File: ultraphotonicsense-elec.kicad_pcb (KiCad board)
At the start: 2 copper layers, 83 x 38 mm, 79 parts, among them J1 Conn_Debug, J10 Conn_01x04, J11 Conn_01x04, J12 Conn_01x04, J13 Conn_01x04, J2 Conn_01x05, J3 Conn_01x05, J4 Conn_01x05, J5 Conn_01x05, J6 Conn_01x05, J7 Conn_01x05, J8 Conn_01x05, J9 Conn_01x05, P1 CAN_conn, P2 CAN_conn, Q1 BSS138, Q2 BSS138, Q3 BSS138, Q4 BSS138, Q5 BSS138, U1 TXB0108PW, U2 74HC164, U3 TCAN332, U4 LD1117S50TR_SOT223, U5 LD1117S33TR_SOT223, U6 LP38693MP-ADJ, U7 STM32F303K8Tx, Y1 Crystal

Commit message: Added RS refs
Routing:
- net GND: track 369.8 -> 380.7 mm, vias 8 -> 10
- net +3V3: track 151.2 -> 152.2 mm
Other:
- net class Default: clearance 0.2 -> 0.4
- rule trace_clearance: 0.2 -> 0.4
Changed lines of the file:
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@@
     (thickness 1.6)
     (drawings 30)
-    (tracks 756)
+    (tracks 763)
     (zones 0)
     (modules 79)
@@
     (user_trace_width 1)
     (user_trace_width 2)
-    (trace_clearance 0.2)
+    (trace_clearance 0.4)
     (zone_clearance 0.508)
     (zone_45_only no)
@@
   (net 61 "Net-(P1-Pad4)")
   (net_class Default "Ceci est la Netclass par défaut."
-    (clearance 0.2)
+    (clearance 0.4)
     (trace_width 0.25)
     (via_dia 0.8)
@@
   (segment (start 58.05 62.75) (end 59.050001 61.749999) (width 1) (layer F.Cu) (net 1))
   (segment (start 59.050001 55.350001) (end 58.55 54.85) (width 1) (layer F.Cu) (net 1))
+  (via (at 49.911107 59.581109) (size 0.8) (drill 0.4) (layers F.Cu B.Cu) (net 1))
+  (segment (start 48.55 62.75) (end 49.911107 61.388893) (width 1) (layer F.Cu) (net 1))
+  (segment (start 49.911107 61.388893) (end 49.911107 59.581109) (width 1) (layer F.Cu) (net 1))
+  (via (at 49.05 52.85) (size 0.8) (drill 0.4) (layers F.Cu B.Cu) (net 1))
+  (segment (start 49.05 52.85) (end 49.05 58.720002) (width 1) (layer B.Cu) (net 1))
+  (segment (start 49.05 58.720002) (end 49.911107 59.581109) (width 1) (layer B.Cu) (net 1))
   (segment (start 56.25 59.15) (end 56.25 52.85) (width 1) (layer F.Cu) (net 2))
   (segment (start 54.45 60.95) (end 56.25 59.15) (width 1) (layer F.Cu) (net 2))
@@
   (via (at 43 60.5) (size 0.8) (drill 0.4) (layers F.Cu B.Cu) (net 2))
   (segment (start 41.4625 60.5) (end 43 60.5) (width 0.25) (layer F.Cu) (net 2))
-  (segment (start 49.58 60.5) (end 51.5 58.58) (width 0.25) (layer B.Cu) (net 2))
-  (segment (start 43 60.5) (end 49.58 60.5) (width 0.25) (layer B.Cu) (net 2))
   (segment (start 72.5 49.5) (end 73.75 48.25) (width 0.25) (layer F.Cu) (net 2))
   (segment (start 74.725 48.725) (end 74.725 49.7) (width 0.25) (layer F.Cu) (net 2))
@@
   (via (at 57.749991 58.948616) (size 0.8) (drill 0.4) (layers F.Cu B.Cu) (net 2))
   (segment (start 58.315676 58.948616) (end 57.749991 58.948616) (width 0.5) (layer B.Cu) (net 2))
+  (segment (start 50.382082 60.899999) (end 51.5 59.782081) (width 0.25) (layer B.Cu) (net 2))
+  (segment (start 51.5 59.782081) (end 51.5 58.58) (width 0.25) (layer B.Cu) (net 2))
+  (segment (start 43.399999 60.899999) (end 50.382082 60.899999) (width 0.25) (layer B.Cu) (net 2))
+  (segment (start 43 60.5) (end 43.399999 60.899999) (width 0.25) (layer B.Cu) (net 2))
   (segment (start 80.371324 41.27501) (end 81.75 39.896334) (width 1) (layer B.Cu) (net 3))
   (segment (start 73.87501 41.27501) (end 80.371324 41.27501) (width 1) (layer B.Cu) (net 3))
@@
   (via (at 75.75001 59.4) (size 0.6) (drill 0.3) (layers F.Cu B.Cu) (net 60))
   (segment (start 75.75001 59.4) (end 74.75 59.4) (width 0.25) (layer F.Cu) (net 60))
-  (segment (start 51.250001 52.124999) (end 48.625001 52.124999) (width 0.25) (layer B.Cu) (net 60))
-  (segment (start 56.25 47) (end 56.25 47.125) (width 0.25) (layer B.Cu) (net 60))
-  (segment (start 56.25 47.125) (end 51.250001 52.124999) (width 0.25) (layer B.Cu) (net 60))
-  (segment (start 48.625001 52.124999) (end 41.25 59.5) (width 0.25) (layer B.Cu) (net 60))
-  (segment (start 41.25 68.474998) (end 43.275002 70.5) (width 0.25) (layer B.Cu) (net 60))
-  (segment (start 41.25 59.5) (end 41.25 68.474998) (width 0.25) (layer B.Cu) (net 60))
   (segment (start 79.07501 62.37501) (end 78.5 61.8) (width 0.25) (layer B.Cu) (net 60))
   (segment (start 82.700726 62.37501) (end 79.07501 62.37501) (width 0.25) (layer B.Cu) (net 60))
@@
   (via (at 51 71.75) (size 0.8) (drill 0.4) (layers F.Cu B.Cu) (net 60))
   (segment (start 53.05 71.75) (end 51 71.75) (width 0.25) (layer F.Cu) (net 60))
-  (segment (start 50 71.75) (end 48.75 70.5) (width 0.25) (layer B.Cu) (net 60))
-  (segment (start 51 71.75) (end 50 71.75) (width 0.25) (layer B.Cu) (net 60))
-  (segment (start 43.275002 70.5) (end 48.75 70.5) (width 0.25) (layer B.Cu) (net 60))
   (segment (start 52.57501 73.32501) (end 68.75 73.32501) (width 0.25) (layer B.Cu) (net 60))
   (segment (start 51 71.75) (end 52.57501 73.32501) (width 0.25) (layer B.Cu) (net 60))
   (segment (start 77.846022 73.32501) (end 68.75 73.32501) (width 0.25) (layer B.Cu) (net 60))
   (segment (start 68.75 73.32501) (end 67.29999 73.32501) (width 0.25) (layer B.Cu) (net 60))
+  (segment (start 56.25 47) (end 56.25 47.125) (width 0.25) (layer B.Cu) (net 60))
+  (segment (start 56.25 47.125) (end 51.550011 51.824989) (width 0.25) (layer B.Cu) (net 60))
+  (segment (start 44.525002 71.75) (end 50.434315 71.75) (width 0.25) (layer B.Cu) (net 60))
+  (segment (start 50.434315 71.75) (end 51 71.75) (width 0.25) (layer B.Cu) (net 60))
+  (segment (start 41.25 68.474998) (end 44.525002 71.75) (width 0.25) (layer B.Cu) (net 60))
+  (segment (start 41.25 59.200416) (end 41.25 68.474998) (width 0.25) (layer B.Cu) (net 60))
+  (segment (start 48.625427 51.824989) (end 41.25 59.200416) (width 0.25) (layer B.Cu) (net 60))
+  (segment (start 51.550011 51.824989) (end 48.625427 51.824989) (width 0.25) (layer B.Cu) (net 60))
   (segment (start 51.25 45.525) (end 51.25 40) (width 0.5) (layer B.Cu) (net 61))
   (segment (start 51.25 47) (end 51.25 45.525) (width 0.5) (layer B.Cu) (net 61))
@@
     (connect_pads (clearance 0.508))
     (min_thickness 0.254)
-    (fill yes (arc_segments 16) (thermal_gap 0.508) (thermal_bridge_width 0.508))
+    (fill (arc_segments 16) (thermal_gap 0.508) (thermal_bridge_width 0.508))
     (polygon
       (pts
@@
     (connect_pads (clearance 0.508))
     (min_thickness 0.254)
-    (fill yes (arc_segments 16) (thermal_gap 0.508) (thermal_bridge_width 0.508))
+    (fill (arc_segments 16) (thermal_gap 0.508) (thermal_bridge_width 0.508))
     (polygon
       (pts

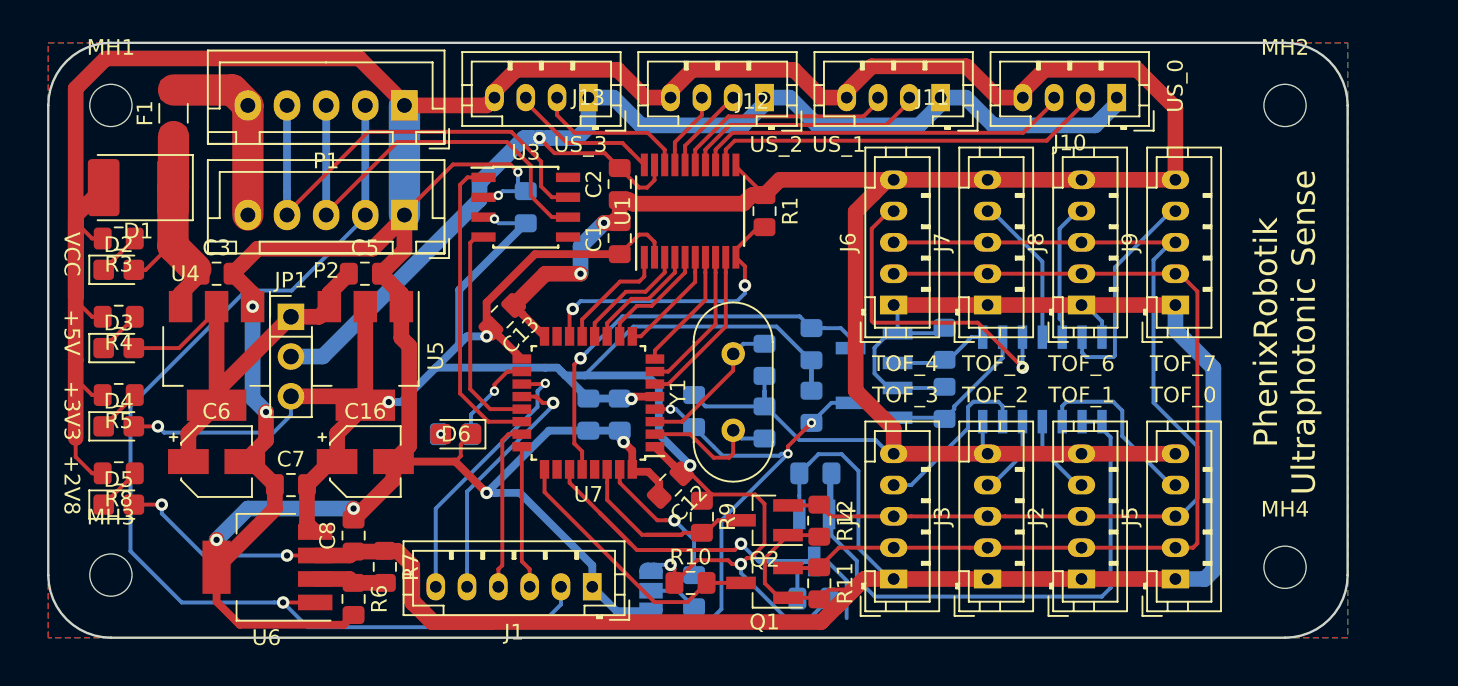
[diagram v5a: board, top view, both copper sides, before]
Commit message: Improved text placement
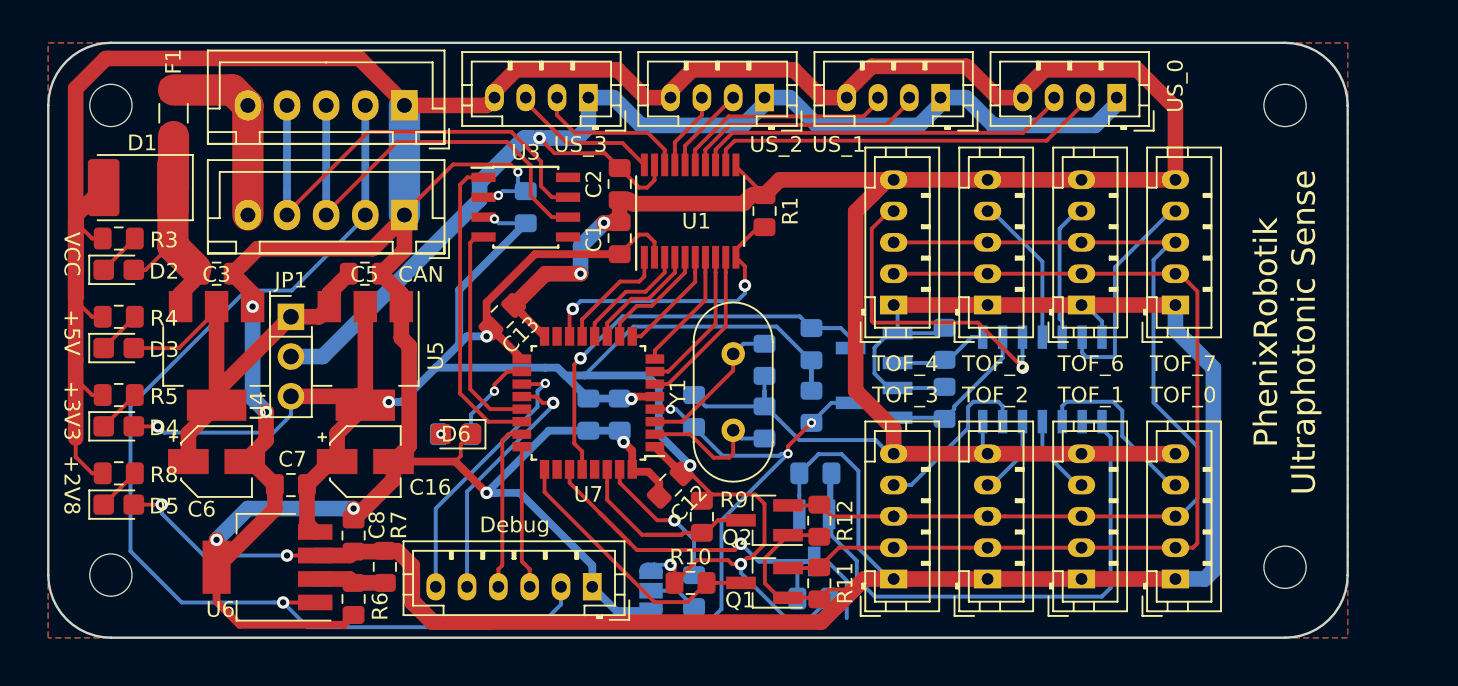
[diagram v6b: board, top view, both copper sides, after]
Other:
- board text added: "CAN"
- board text added: "Debug"

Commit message: Rename phoenix phenix. Connect mounting holes to gnd.
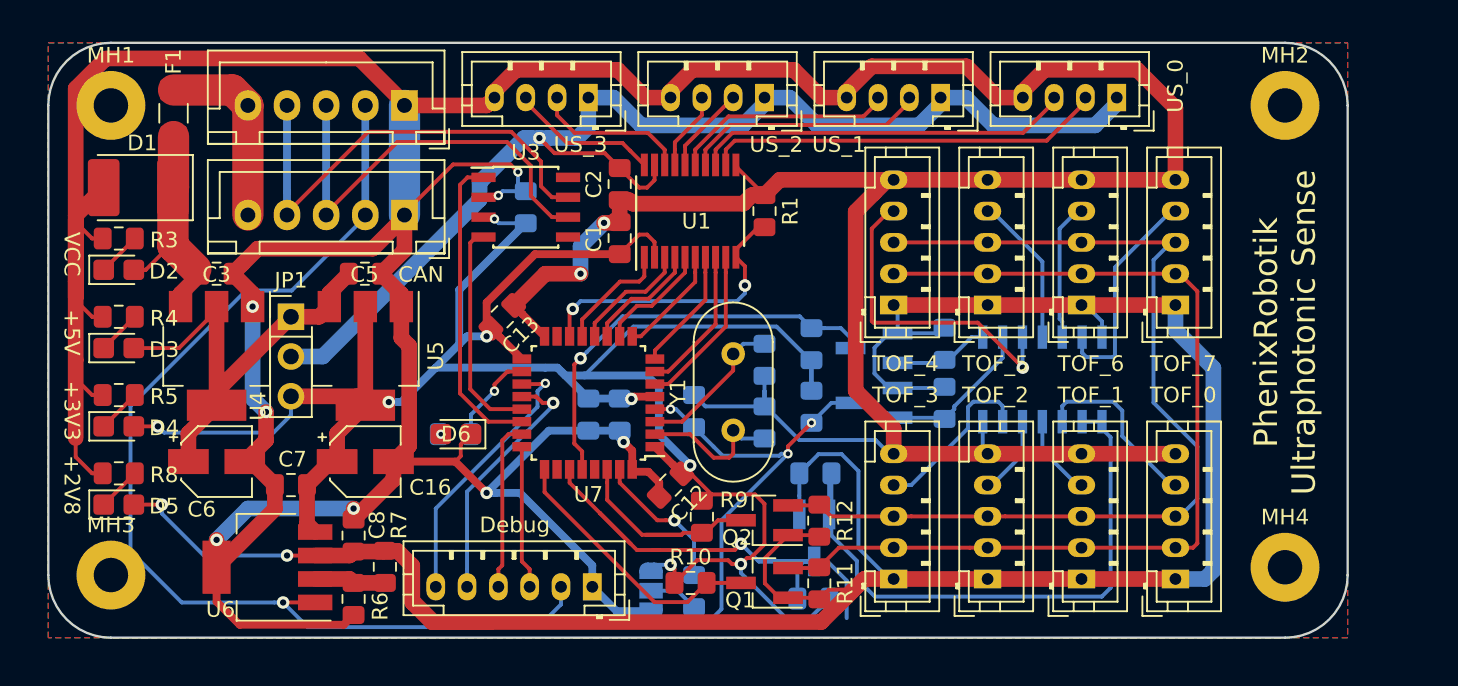
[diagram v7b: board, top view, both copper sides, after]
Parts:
- C1, C11, C12, C13, C14, C2: value C -> 100n
- C10, C9: value C -> 26p
- C15: value C -> 1µ
- C4: value 100nF -> 100n
- MH1, MH2, MH3, MH4: value MountingHole -> MountingHole_Pad; footprint MountingHole:MountingHole_2.7mm_M2.5 -> MountingHole:MountingHole_2.2mm_M2_Pad
- R15: value R -> 10k
- R16: value R -> 1k
- renumbered REF** to #LOGO1, REF** to #LOGO2, REF** to #LOGO3
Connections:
- C14 pad 1: +3V3 -> GND
- C14 pad 2: GND -> +3V3
- MH1 pad 1: (no net) -> GND
- MH2 pad 1: (no net) -> GND
- MH3 pad 1: (no net) -> GND
- MH4 pad 1: (no net) -> GND
- U3 pad 5: (no net) -> Net-(U3-Pad5)
- U3 pad 8: (no net) -> Net-(U3-Pad8)
- U7 pad 15: (no net) -> Net-(U7-Pad15)
- U7 pad 26: (no net) -> Net-(U7-Pad26)
- U7 pad 29: (no net) -> Net-(U7-Pad29)

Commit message: fix drc
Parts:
- turned C14 to 90 degrees
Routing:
- net +2V8: track 167.1 -> 165.8 mm
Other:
- net class Default: clearance 0.4 -> 0.2
- rule trace_clearance: 0.4 -> 0.2
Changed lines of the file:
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@@
     (thickness 1.6)
     (drawings 32)
-    (tracks 763)
+    (tracks 758)
     (zones 0)
     (modules 79)
@@
     (user_trace_width 1)
     (user_trace_width 2)
-    (trace_clearance 0.4)
+    (trace_clearance 0.2)
     (zone_clearance 0.508)
     (zone_45_only no)
@@
   (net 66 "Net-(U7-Pad29)")
   (net_class Default "Ceci est la Netclass par défaut."
-    (clearance 0.4)
+    (clearance 0.2)
     (trace_width 0.25)
     (via_dia 0.8)
@@
   )
   (module Capacitor_SMD:C_0805_2012Metric_Pad1.15x1.40mm_HandSolder (layer B.Cu)
-    (at 70.5 59.75 270)
+    (at 70.5 59.75 90)
     (descr "Capacitor SMD 0805 (2012 Metric), square (rectangular) end terminal, IPC_7351 nominal with elongated pad for handsoldering. (Body size source: https://docs.google.com/spreadsheets/d/1BsfQQcO9C6DZCsRaXUlFlo91Tg2WpOkGARC1WS5S8t0/edit?usp=sharing), generated with kicad-footprint-generator")
     (tags "capacitor handsolder")
     (attr smd)
-    (fp_text reference C14 (at -3.75 -0.1 270) (layer B.SilkS)
+    (fp_text reference C14 (at -3.75 -0.1 90) (layer B.SilkS)
       (effects (font (size 1 1) (thickness 0.15)) (justify mirror))
     )
-    (fp_text value 100n (at 0 -1.65 270) (layer B.Fab)
+    (fp_text value 100n (at 0 -1.65 90) (layer B.Fab)
       (effects (font (size 1 1) (thickness 0.15)) (justify mirror))
     )
@@
     (fp_line (start 1.85 0.95) (end 1.85 -0.95) (layer B.CrtYd) (width 0.05))
     (fp_line (start 1.85 -0.95) (end -1.85 -0.95) (layer B.CrtYd) (width 0.05))
-    (fp_text user %R (at 0 0 270) (layer B.Fab)
+    (fp_text user %R (at 0 0 90) (layer B.Fab)
       (effects (font (size 0.5 0.5) (thickness 0.08)) (justify mirror))
     )
-    (pad 1 smd roundrect (at -1.025 0 270) (size 1.15 1.4) (layers B.Cu B.Paste B.Mask) (roundrect_rratio 0.217391)
+    (pad 1 smd roundrect (at -1.025 0 90) (size 1.15 1.4) (layers B.Cu B.Paste B.Mask) (roundrect_rratio 0.217391)
       (net 1 GND))
-    (pad 2 smd roundrect (at 1.025 0 270) (size 1.15 1.4) (layers B.Cu B.Paste B.Mask) (roundrect_rratio 0.217391)
+    (pad 2 smd roundrect (at 1.025 0 90) (size 1.15 1.4) (layers B.Cu B.Paste B.Mask) (roundrect_rratio 0.217391)
       (net 2 +3V3))
     (model ${KISYS3DMOD}/Capacitor_SMD.3dshapes/C_0805_2012Metric.wrl
@@
   (via (at 43.25 65.5) (size 0.8) (drill 0.4) (layers F.Cu B.Cu) (net 6))
   (segment (start 43.25 65.5) (end 41.4625 65.5) (width 0.25) (layer F.Cu) (net 6))
-  (segment (start 46.325427 68.775009) (end 46.300418 68.75) (width 0.25) (layer B.Cu) (net 6))
-  (segment (start 47.174573 68.775009) (end 46.325427 68.775009) (width 0.25) (layer B.Cu) (net 6))
-  (segment (start 47.174573 68.775009) (end 47.199582 68.75) (width 0.25) (layer B.Cu) (net 6))
-  (segment (start 47.199582 68.75) (end 51.25 68.75) (width 0.25) (layer B.Cu) (net 6))
-  (segment (start 45.959324 68.775009) (end 47.174573 68.775009) (width 0.25) (layer B.Cu) (net 6))
-  (segment (start 43.25 66.065685) (end 45.959324 68.775009) (width 0.25) (layer B.Cu) (net 6))
-  (segment (start 43.25 65.5) (end 43.25 66.065685) (width 0.25) (layer B.Cu) (net 6))
   (segment (start 59.24999 69.89999) (end 59.24999 71.74999) (width 1) (layer F.Cu) (net 6))
   (segment (start 59.24999 71.74999) (end 60.5 73) (width 1) (layer F.Cu) (net 6))
@@
   (segment (start 64.25 73) (end 85.375 73) (width 1) (layer F.Cu) (net 6))
   (segment (start 60.5 73) (end 64.25 73) (width 1) (layer F.Cu) (net 6))
+  (segment (start 46.5 68.75) (end 43.25 65.5) (width 0.25) (layer B.Cu) (net 6))
+  (segment (start 51.25 68.75) (end 46.5 68.75) (width 0.25) (layer B.Cu) (net 6))
   (segment (start 80.275 61.275) (end 79.75 60.75) (width 0.25) (layer B.Cu) (net 7))
   (segment (start 81.75 61.275) (end 80.275 61.275) (width 0.25) (layer B.Cu) (net 7))
@@
   (segment (start 77.846022 73.32501) (end 68.75 73.32501) (width 0.25) (layer B.Cu) (net 60))
   (segment (start 68.75 73.32501) (end 67.29999 73.32501) (width 0.25) (layer B.Cu) (net 60))
-  (segment (start 56.25 47) (end 56.25 47.125) (width 0.25) (layer B.Cu) (net 60))
-  (segment (start 56.25 47.125) (end 51.550011 51.824989) (width 0.25) (layer B.Cu) (net 60))
-  (segment (start 44.525002 71.75) (end 50.434315 71.75) (width 0.25) (layer B.Cu) (net 60))
-  (segment (start 50.434315 71.75) (end 51 71.75) (width 0.25) (layer B.Cu) (net 60))
-  (segment (start 41.25 68.474998) (end 44.525002 71.75) (width 0.25) (layer B.Cu) (net 60))
-  (segment (start 41.25 59.200416) (end 41.25 68.474998) (width 0.25) (layer B.Cu) (net 60))
-  (segment (start 48.625427 51.824989) (end 41.25 59.200416) (width 0.25) (layer B.Cu) (net 60))
-  (segment (start 51.550011 51.824989) (end 48.625427 51.824989) (width 0.25) (layer B.Cu) (net 60))
+  (segment (start 51 71.75) (end 47.95 71.75) (width 0.25) (layer B.Cu) (net 60))
+  (segment (start 56.25 47.125) (end 56.25 47) (width 0.25) (layer B.Cu) (net 60))
+  (segment (start 51 71.75) (end 48.35 71.75) (width 0.25) (layer B.Cu) (net 60))
+  (segment (start 48.35 71.75) (end 42.2 65.6) (width 0.25) (layer B.Cu) (net 60))
+  (segment (start 48.625427 51.824989) (end 51.550011 51.824989) (width 0.25) (layer B.Cu) (net 60))
+  (segment (start 42.2 65.6) (end 42.2 58.250416) (width 0.25) (layer B.Cu) (net 60))
+  (segment (start 42.2 58.250416) (end 48.625427 51.824989) (width 0.25) (layer B.Cu) (net 60))
+  (segment (start 51.550011 51.824989) (end 56.25 47.125) (width 0.25) (layer B.Cu) (net 60))
   (segment (start 51.25 45.525) (end 51.25 40) (width 0.5) (layer B.Cu) (net 61))
   (segment (start 51.25 47) (end 51.25 45.525) (width 0.5) (layer B.Cu) (net 61))
@@
     (connect_pads (clearance 0.508))
     (min_thickness 0.254)
-    (fill (arc_segments 16) (thermal_gap 0.508) (thermal_bridge_width 0.508))
+    (fill yes (arc_segments 16) (thermal_gap 0.508) (thermal_bridge_width 0.508))
     (polygon
       (pts
@@
     (connect_pads (clearance 0.508))
     (min_thickness 0.254)
-    (fill (arc_segments 16) (thermal_gap 0.508) (thermal_bridge_width 0.508))
+    (fill yes (arc_segments 16) (thermal_gap 0.508) (thermal_bridge_width 0.508))
     (polygon
       (pts
